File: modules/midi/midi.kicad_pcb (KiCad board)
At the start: 2 copper layers, 30.5 x 68.6 mm, 4 parts

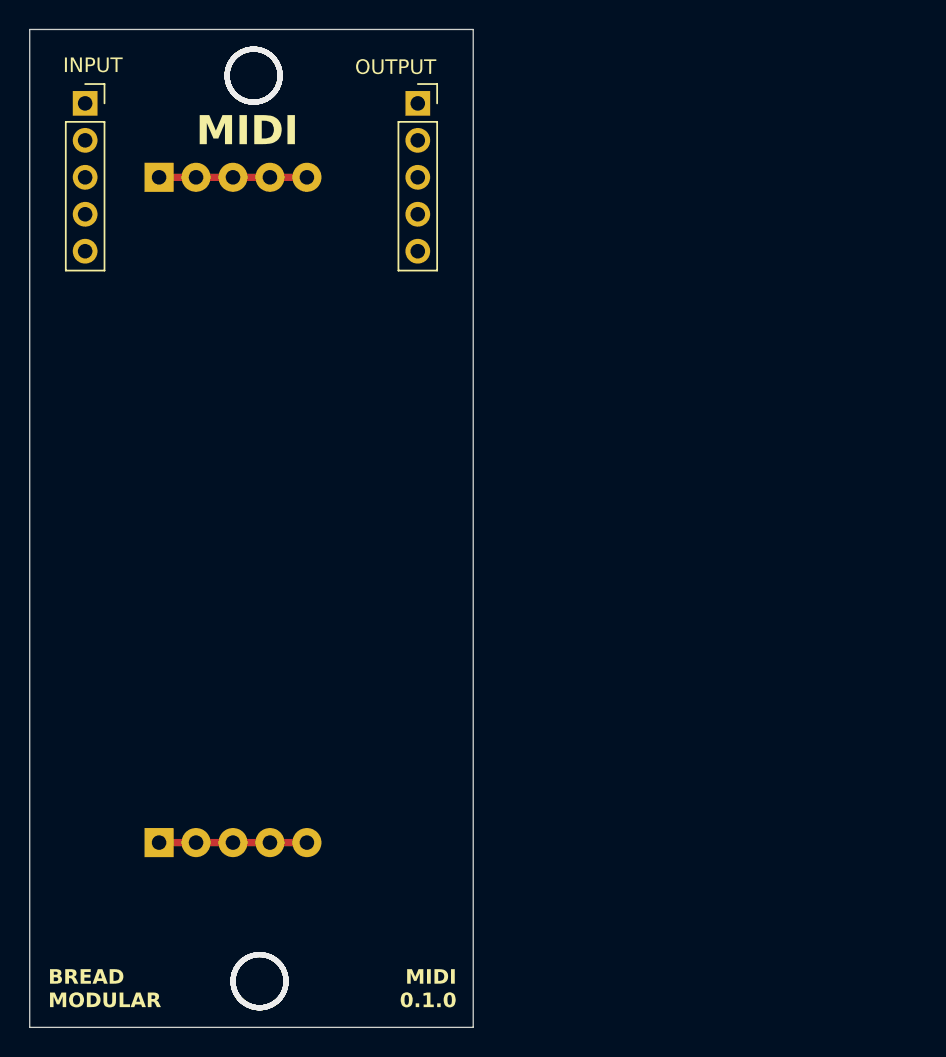
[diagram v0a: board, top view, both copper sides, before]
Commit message: Add MIDI PCB
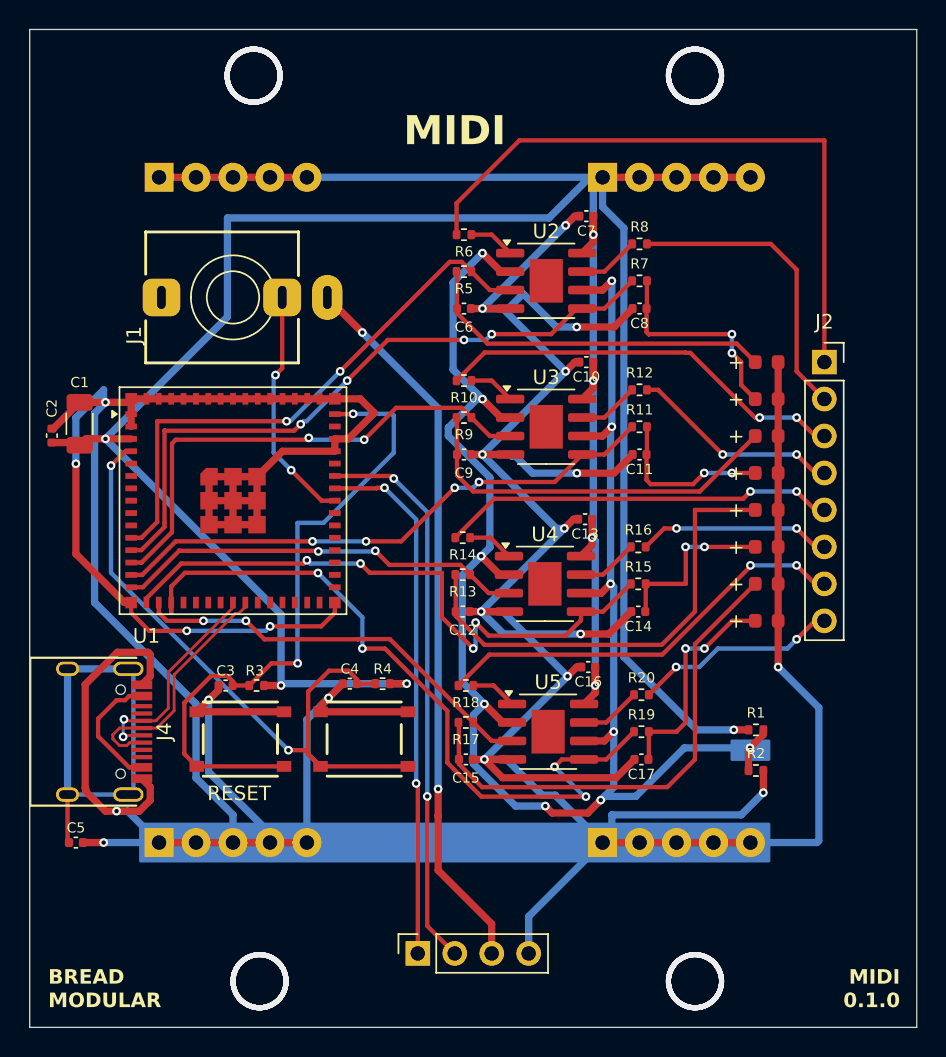
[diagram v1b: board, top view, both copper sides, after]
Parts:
- removed INPUT1, OUTPUT1: Conn_01x05_Socket, Connector_PinSocket_2.54mm:PinSocket_1x05_P2.54mm_Vertical
- added C1: 100uf, Capacitor_SMD:C_1206_3216Metric, F.Cu at (50.4, 67.7)
- added C10: 0.1uf, Capacitor_SMD:C_0402_1005Metric, F.Cu at (85.2, 63.5)
- added C11: 0.1uf, Capacitor_SMD:C_0402_1005Metric, F.Cu at (88.9, 69.8)
- added C12: 0.1uf, Capacitor_SMD:C_0402_1005Metric, F.Cu at (76.7, 80.6)
- added C13: 0.1uf, Capacitor_SMD:C_0402_1005Metric, F.Cu at (85.2, 74.3)
- added C14: 0.1uf, Capacitor_SMD:C_0402_1005Metric, F.Cu at (88.8, 80.6)
- added C15: 0.1uf, Capacitor_SMD:C_0402_1005Metric, F.Cu at (77.0, 90.8)
- added C16: 0.1uf, Capacitor_SMD:C_0402_1005Metric, F.Cu at (85.4, 84.5)
- added C17: 0.1uf, Capacitor_SMD:C_0402_1005Metric, F.Cu at (89.0, 90.8)
- added C2: 0.1uf, Capacitor_SMD:C_0402_1005Metric, F.Cu at (48.5, 68.6)
- added C3: 0.1uf, Capacitor_SMD:C_0402_1005Metric, F.Cu at (60.5, 85.7)
- added C4: 0.1uf, Capacitor_SMD:C_0402_1005Metric, F.Cu at (69.0, 85.6)
- added C5: 0.1uf, Capacitor_SMD:C_0402_1005Metric, F.Cu at (50.2, 96.5)
- added C6: 0.1uf, Capacitor_SMD:C_0402_1005Metric, F.Cu at (76.8, 59.8)
- added C7: 0.1uf, Capacitor_SMD:C_0402_1005Metric, F.Cu at (85.2, 53.5)
- added C8: 0.1uf, Capacitor_SMD:C_0402_1005Metric, F.Cu at (88.9, 59.8)
- added C9: 0.1uf, Capacitor_SMD:C_0402_1005Metric, F.Cu at (76.8, 69.8)
- added D1: LED, LED_SMD:LED_0603_1608Metric, F.Cu at (97.6, 63.5)
- added D2: LED, LED_SMD:LED_0603_1608Metric, F.Cu at (97.6, 66.0)
- added D3: LED, LED_SMD:LED_0603_1608Metric, F.Cu at (97.6, 68.6)
- added D4: LED, LED_SMD:LED_0603_1608Metric, F.Cu at (97.6, 71.1)
- added D5: LED, LED_SMD:LED_0603_1608Metric, F.Cu at (97.6, 73.7)
- added D6: LED, LED_SMD:LED_0603_1608Metric, F.Cu at (97.6, 76.2)
- added D7: LED, LED_SMD:LED_0603_1608Metric, F.Cu at (97.6, 78.7)
- added D8: LED, LED_SMD:LED_0603_1608Metric, F.Cu at (97.6, 81.3)
- added GND2: Conn_01x05_Pin, BreadModular_MISC:Power_Connector, B.Cu at (86.4, 96.5)
- added J1: AudioJack3, BreadModular_AudioJacks:Jack_3.5mm_QingPu_WQP-PJ366ST_Vertical, F.Cu at (61.0, 59.1)
- added J2: GATE_OUTS, Connector_PinSocket_2.54mm:PinSocket_1x08_P2.54mm_Vertical, F.Cu at (101.6, 63.5)
- added J3: CONFIG, Connector_PinSocket_2.54mm:PinSocket_1x04_P2.54mm_Vertical, F.Cu at (73.7, 104.1)
- added J4: USB_C_Receptacle_USB2.0_16P, BreadModular_TypeC:HRO-TYPE-C-31-M-12, F.Cu at (47.0, 88.9)
- added R1: 1k, Resistor_SMD:R_0402_1005Metric, F.Cu at (96.9, 88.8)
- added R10: 1k, Resistor_SMD:R_0402_1005Metric, F.Cu at (76.8, 64.8)
- added R11: 2k, Resistor_SMD:R_0402_1005Metric, F.Cu at (88.9, 67.9)
- added R12: 1k, Resistor_SMD:R_0402_1005Metric, F.Cu at (88.9, 65.4)
- added R13: 2k, Resistor_SMD:R_0402_1005Metric, F.Cu at (76.7, 78.1)
- added R14: 1k, Resistor_SMD:R_0402_1005Metric, F.Cu at (76.7, 75.6)
- added R15: 2k, Resistor_SMD:R_0402_1005Metric, F.Cu at (88.8, 78.7)
- added R16: 1k, Resistor_SMD:R_0402_1005Metric, F.Cu at (88.8, 76.2)
- added R17: 2k, Resistor_SMD:R_0402_1005Metric, F.Cu at (77.0, 88.3)
- added R18: 1k, Resistor_SMD:R_0402_1005Metric, F.Cu at (77.0, 85.7)
- added R19: 2k, Resistor_SMD:R_0402_1005Metric, F.Cu at (89.0, 88.9)
- added R2: 1k, Resistor_SMD:R_0402_1005Metric, F.Cu at (96.9, 91.6)
- added R20: 1k, Resistor_SMD:R_0402_1005Metric, F.Cu at (89.0, 86.4)
- added R3: 10K, Resistor_SMD:R_0402_1005Metric, F.Cu at (62.6, 85.7)
- added R4: 10K, Resistor_SMD:R_0402_1005Metric, F.Cu at (71.2, 85.6)
- added R5: 2k, Resistor_SMD:R_0402_1005Metric, F.Cu at (76.8, 57.3)
- added R6: 1k, Resistor_SMD:R_0402_1005Metric, F.Cu at (76.8, 54.7)
- added R7: 2k, Resistor_SMD:R_0402_1005Metric, F.Cu at (88.9, 57.9)
- added R8: 1k, Resistor_SMD:R_0402_1005Metric, F.Cu at (88.9, 55.4)
- added R9: 2k, Resistor_SMD:R_0402_1005Metric, F.Cu at (76.8, 67.3)
- added SW1: RESET, BreadModular_MISC:SPST_TS-1187A-B-A-B, F.Cu at (61.5, 89.4)
- added SW2: BOOT, BreadModular_MISC:SPST_TS-1187A-B-A-B, F.Cu at (70.0, 89.4)
- added U1: ESP32-S3-MINI-1U, RF_Module:ESP32-S2-MINI-1U, F.Cu at (61.0, 73.0)
- added U2: MCP6002-xSN, Package_SO:SOIC-8-1EP_3.9x4.9mm_P1.27mm_EP2.29x3mm, F.Cu at (82.5, 57.9)
- added U3: MCP6002-xSN, Package_SO:SOIC-8-1EP_3.9x4.9mm_P1.27mm_EP2.29x3mm, F.Cu at (82.5, 67.9)
- added U4: MCP6002-xSN, Package_SO:SOIC-8-1EP_3.9x4.9mm_P1.27mm_EP2.29x3mm, F.Cu at (82.4, 78.7)
- added U5: MCP6002-xSN, Package_SO:SOIC-8-1EP_3.9x4.9mm_P1.27mm_EP2.29x3mm, F.Cu at (82.6, 88.9)
- added V_SUPPLY2: Conn_01x05_Pin, BreadModular_MISC:Power_Connector, B.Cu at (86.4, 50.8)
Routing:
- net GND: track 10.2 -> 431.9 mm, vias 0 -> 21
- net V_SUPPLY: track 10.2 -> 215.8 mm, vias 0 -> 8
- net V_MID: track 0.00 -> 121.4 mm, vias 0 -> 11
- net /esp32/GATE_8: track 0.00 -> 50.6 mm, vias 0 -> 4
- net MIDI_GND: track 0.00 -> 49.8 mm, vias 0 -> 2
- net Net-(SW2-B): track 0.00 -> 46.3 mm, vias 0 -> 2
- net /esp32/GATE_2: track 0.00 -> 46.0 mm, vias 0 -> 4
- net Net-(SW1-B): track 0.00 -> 45.3 mm, vias 0 -> 2
- net /gate_process/GATE_A_OUT: track 0.00 -> 44.5 mm
- net /esp32/GATE_6: track 0.00 -> 42.8 mm, vias 0 -> 4
- net /esp32/GATE_1: track 0.00 -> 38.8 mm, vias 0 -> 2
- net /esp32/GATE_4: track 0.00 -> 38.6 mm, vias 0 -> 4
- net RX: track 0.00 -> 38.5 mm, vias 0 -> 2
- net TX: track 0.00 -> 36.4 mm, vias 0 -> 2
- net /esp32/GATE_3: track 0.00 -> 34.9 mm, vias 0 -> 2
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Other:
- board size 30.5 x 68.6 mm -> 61 x 68.6 mm
- board text added: "RESET"
- board text removed: "INPUT"
- board text removed: "OUTPUT"

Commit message: Finalized the midi module.
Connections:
- R6 pad 1: unconnected-(R6-Pad1) -> Net-(R6-Pad1)
- R8 pad 1: unconnected-(R8-Pad1) -> Net-(R8-Pad1)
- U2 pad 1: unconnected-(R6-Pad1) -> Net-(R6-Pad1)
- U2 pad 7: unconnected-(R8-Pad1) -> Net-(R8-Pad1)
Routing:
- net GND: track 431.9 -> 438.6 mm
- net V_MID: track 121.4 -> 125.8 mm
- net unconnected-(R8-Pad1): track 4.22 -> 0.00 mm
- net Net-(R8-Pad1): track 0.00 -> 4.22 mm
- net unconnected-(R6-Pad1): track 3.19 -> 0.00 mm
- net Net-(R6-Pad1): track 0.00 -> 3.19 mm
- net Net-(U1-IO19): track 15.1 -> 17.0 mm
- net Net-(U1-IO20): track 17.0 -> 15.3 mm
- net Net-(D4-A): track 11.6 -> 12.9 mm
- net Net-(D5-A): track 32.2 -> 33.4 mm
- net Net-(D2-A): track 14.6 -> 15.7 mm
- net /esp32/GATE_8: track 50.6 -> 51.6 mm
- net /esp32/GATE_4: track 38.6 -> 39.5 mm
- net Net-(D3-A): track 26.5 -> 27.3 mm
- net /esp32/GATE_2: track 46.0 -> 46.7 mm
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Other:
- board text added: "1"
- board text added: "2"
- board text added: "3"
- board text added: "4"
- board text added: "5"
- board text added: "6"
- board text added: "7"
- board text added: "8"
- board text added: "GATE CHANNEL"

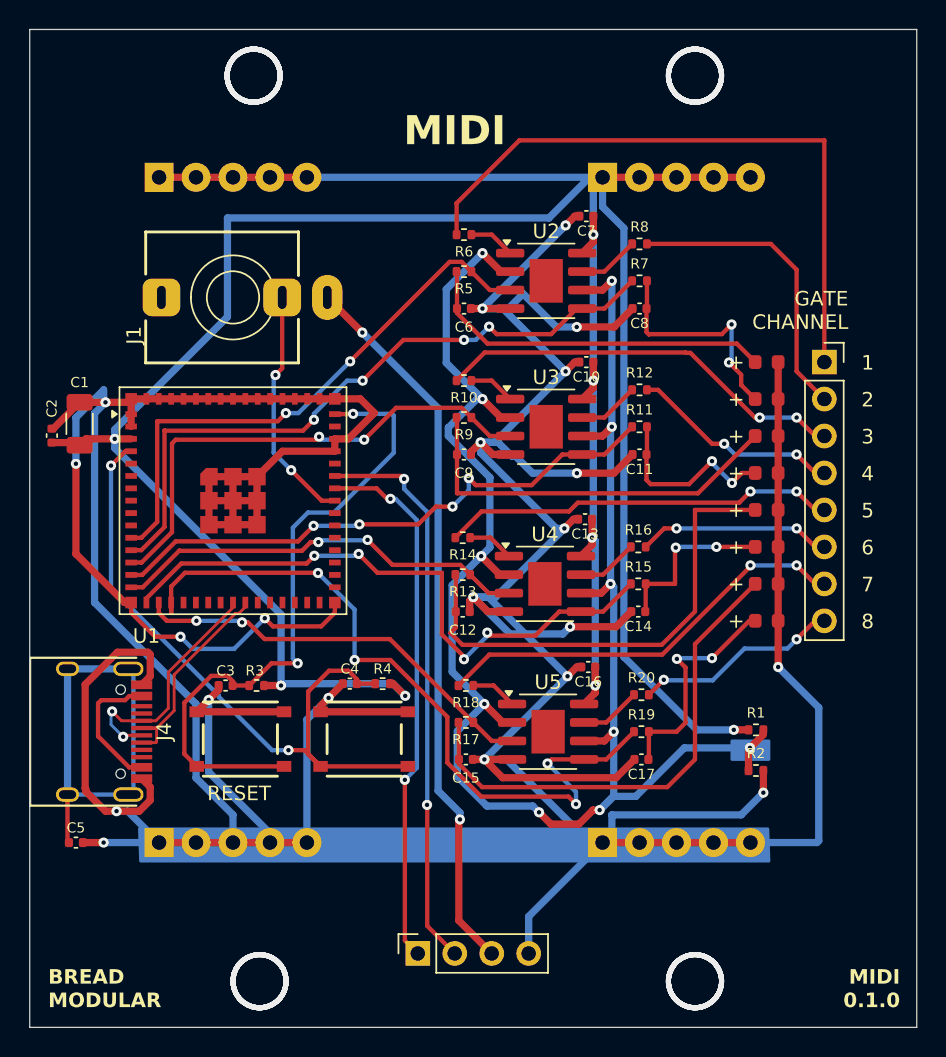
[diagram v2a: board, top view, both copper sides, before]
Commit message: Implement the PCB layout and routing
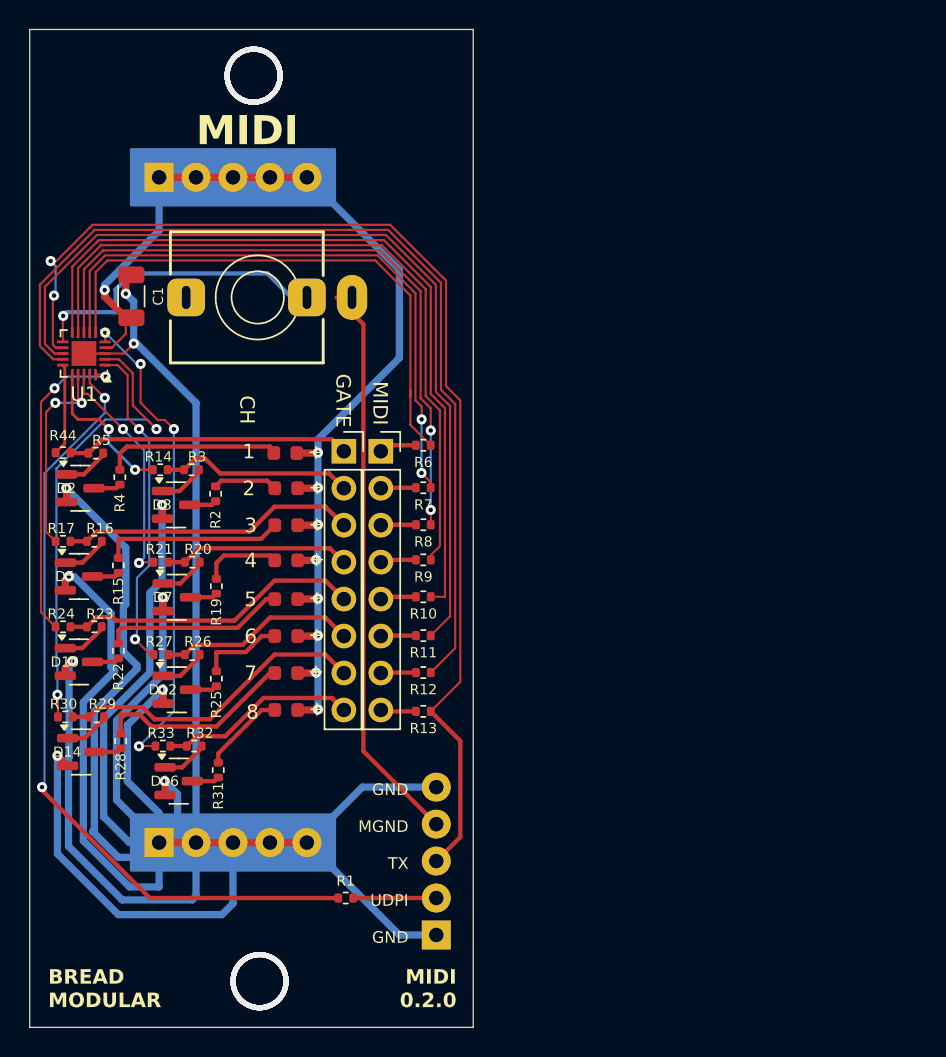
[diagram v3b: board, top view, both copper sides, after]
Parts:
- removed C10, C11, C12, C13, C14, C15, C16, C17, C2, C3, C4, C5, C6, C7, C8, C9: 0.1uf, Capacitor_SMD:C_0402_1005Metric
- removed GND2, V_SUPPLY2: Conn_01x05_Pin, BreadModular_MISC:Power_Connector
- removed J2: GATE_OUTS, Connector_PinSocket_2.54mm:PinSocket_1x08_P2.54mm_Vertical
- removed J3: CONFIG, Connector_PinSocket_2.54mm:PinSocket_1x04_P2.54mm_Vertical
- removed J4: USB_C_Receptacle_USB2.0_16P, BreadModular_TypeC:HRO-TYPE-C-31-M-12
- removed R18: 1k, Resistor_SMD:R_0402_1005Metric
- removed SW1: RESET, BreadModular_MISC:SPST_TS-1187A-B-A-B
- removed SW2: BOOT, BreadModular_MISC:SPST_TS-1187A-B-A-B
- removed U2, U3, U4, U5: MCP6002-xSN, Package_SO:SOIC-8-1EP_3.9x4.9mm_P1.27mm_EP2.29x3mm
- added CONFIG1: Conn_01x05_Pin, BreadModular_MISC:Power_Connector, B.Cu at (74.9, 102.9)
- added D10: SS8050, Package_TO_SOT_SMD:SOT-23, F.Cu at (50.4, 84.1)
- added D100: LED, LED_SMD:LED_0603_1608Metric, F.Cu at (64.6, 69.8)
- added D11: LED, LED_SMD:LED_0603_1608Metric, F.Cu at (64.6, 82.3)
- added D12: SS8050, Package_TO_SOT_SMD:SOT-23, F.Cu at (57.1, 86.0)
- added D13: LED, LED_SMD:LED_0603_1608Metric, F.Cu at (64.6, 84.9)
- added D14: SS8050, Package_TO_SOT_SMD:SOT-23, F.Cu at (50.5, 90.3)
- added D15: LED, LED_SMD:LED_0603_1608Metric, F.Cu at (64.6, 87.4)
- added D16: SS8050, Package_TO_SOT_SMD:SOT-23, F.Cu at (57.2, 92.3)
- added OUTPUT1: GATE_OUT, Connector_PinSocket_2.54mm:PinSocket_1x08_P2.54mm_Vertical, F.Cu at (68.6, 69.6)
- added OUTPUT2: MIDI_OUT, Connector_PinSocket_2.54mm:PinSocket_1x08_P2.54mm_Vertical, F.Cu at (71.1, 69.6)
- added R21: 1k, Resistor_SMD:R_0402_1005Metric, F.Cu at (56.0, 77.2)
- added R22: 1k, Resistor_SMD:R_0402_1005Metric, F.Cu at (53.1, 83.3)
- added R23: 10k, Resistor_SMD:R_0402_1005Metric, F.Cu at (51.4, 81.7)
- added R24: 1k, Resistor_SMD:R_0402_1005Metric, F.Cu at (49.3, 81.7)
- added R25: 1k, Resistor_SMD:R_0402_1005Metric, F.Cu at (59.8, 85.3)
- added R26: 10k, Resistor_SMD:R_0402_1005Metric, F.Cu at (58.2, 83.6)
- added R27: 1k, Resistor_SMD:R_0402_1005Metric, F.Cu at (56.0, 83.6)
- added R28: 1k, Resistor_SMD:R_0402_1005Metric, F.Cu at (53.2, 89.5)
- added R29: 10k, Resistor_SMD:R_0402_1005Metric, F.Cu at (51.6, 87.9)
- added R30: 1k, Resistor_SMD:R_0402_1005Metric, F.Cu at (49.4, 87.9)
- added R31: 1k, Resistor_SMD:R_0402_1005Metric, F.Cu at (59.9, 91.5)
- added R32: 10k, Resistor_SMD:R_0402_1005Metric, F.Cu at (58.3, 89.9)
- added R33: 1k, Resistor_SMD:R_0402_1005Metric, F.Cu at (56.1, 89.9)
- added R44: 1k, Resistor_SMD:R_0402_1005Metric, F.Cu at (49.3, 69.7)
- D2, D3, D5, D7: value LED -> SS8050; footprint LED_SMD:LED_0603_1608Metric -> Package_TO_SOT_SMD:SOT-23
- J1: value AudioJack3 -> MIDI_IN
- R1: value 1k -> 4.7k
- R11, R13, R15, R17, R19, R7, R9: value 2k -> 1k
- R16, R20: value 1k -> 10k
- R3: value 10K -> 10k
- R4: value 10K -> 1k
- R5: value 2k -> 10k
- U1: value ESP32-S3-MINI-1U -> ATtiny1616-M; footprint RF_Module:ESP32-S2-MINI-1U -> Package_DFN_QFN:VQFN-20-1EP_3x3mm_P0.4mm_EP1.7x1.7mm
- moved D2 47.6 mm to (50.5, 72.2), turned to 0 degrees
- moved D5 47.5 mm to (50.4, 78.2), turned to 0 degrees
- moved R2 41.7 mm to (59.8, 72.6), turned to 90 degrees
- moved D3 40.9 mm to (57.1, 73.3), turned to 0 degrees
- moved D7 40.5 mm to (57.1, 79.7), turned to 0 degrees
- moved R16 37.4 mm to (51.4, 75.8)
- moved R15 35.7 mm to (53.1, 77.5), turned to 90 degrees
- moved D1 34.1 mm to (64.6, 72.2), turned to 0 degrees
- moved D4 33.2 mm to (64.6, 74.7), turned to 0 degrees
- moved D8 33.1 mm to (64.6, 79.8), turned to 0 degrees
- moved D6 33.0 mm to (64.6, 77.1), turned to 0 degrees
- moved R20 32.2 mm to (58.2, 77.2)
- moved R19 30.9 mm to (59.8, 78.9), turned to 90 degrees
- moved R1 30.5 mm to (68.7, 100.3)
- moved R17 30.4 mm to (49.3, 75.8), turned to 0 degrees
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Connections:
- net /esp32/GATE_7 renamed GATE_3
- C1 pad 1: V_SUPPLY -> GND
- C1 pad 2: GND -> V_SUPPLY
- D1 pad 1: GND -> Net-(D1-K)
- D1 pad 2: Net-(D1-A) -> V_SUPPLY
- D2 pad 1: GND -> Net-(D2-K-Pad1)
- D2 pad 2: Net-(D2-A) -> GND
- D3 pad 1: GND -> Net-(D3-K-Pad1)
- D3 pad 2: Net-(D3-A) -> GND
- D4 pad 1: GND -> Net-(D4-K)
- D4 pad 2: Net-(D4-A) -> V_SUPPLY
- D5 pad 1: GND -> Net-(D5-K-Pad1)
- D5 pad 2: Net-(D5-A) -> GND
- D6 pad 1: GND -> Net-(D6-K)
- D6 pad 2: Net-(D6-A) -> V_SUPPLY
- D7 pad 1: GND -> Net-(D7-K-Pad1)
- D7 pad 2: Net-(D7-A) -> GND
- D8 pad 1: GND -> Net-(D8-K)
- D8 pad 2: Net-(D8-A) -> V_SUPPLY
- J1 pad R: /esp32/MIDI_IN -> MIDI_IN
- J1 pad S: MIDI_GND -> MIDI_GROUND
- R1 pad 1: V_SUPPLY -> Net-(U1-~{RESET}/PA0)
- R1 pad 2: V_MID -> UDPI
- R10 pad 1: Net-(R10-Pad1) -> MIDI_OUT_5
- R10 pad 2: /gate_process1/GATE_A_OUT -> Net-(OUTPUT2-Pin_5)
- R11 pad 1: /esp32/GATE_4 -> MIDI_OUT_6
- R11 pad 2: Net-(D4-A) -> Net-(OUTPUT2-Pin_6)
- R12 pad 1: Net-(R12-Pad1) -> MIDI_OUT_7
- R12 pad 2: /gate_process1/GATE_B_OUT -> Net-(OUTPUT2-Pin_7)
- R13 pad 1: /esp32/GATE_5 -> TX
- R13 pad 2: Net-(D5-A) -> Net-(OUTPUT2-Pin_8)
- R14 pad 1: Net-(R14-Pad1) -> GATE_2
- R14 pad 2: /gate_process2/GATE_A_OUT -> /Gate Out1/GATE_OUT
- R15 pad 1: /esp32/GATE_6 -> Net-(D5-A)
- R15 pad 2: Net-(D6-A) -> Net-(D4-K)
- R16 pad 1: Net-(R16-Pad1) -> /Gate Out2/GATE_OUT
- R16 pad 2: /gate_process2/GATE_B_OUT -> Net-(D5-K-Pad1)
- R17 pad 2: Net-(D7-A) -> /Gate Out2/GATE_OUT
- R19 pad 1: /esp32/GATE_8 -> Net-(D7-A)
- R19 pad 2: Net-(D8-A) -> Net-(D6-K)
- R2 pad 1: V_MID -> Net-(D3-A)
- R2 pad 2: GND -> Net-(D1-K)
- R20 pad 1: Net-(R20-Pad1) -> /Gate Out3/GATE_OUT
- R20 pad 2: /gate_process3/GATE_B_OUT -> Net-(D7-K-Pad1)
- R3 pad 1: V_SUPPLY -> /Gate Out1/GATE_OUT
- R3 pad 2: Net-(SW1-B) -> Net-(D3-K-Pad1)
- R4 pad 1: V_SUPPLY -> Net-(D2-A)
- R4 pad 2: Net-(SW2-B) -> Net-(D100-K)
- R5 pad 1: /esp32/GATE_1 -> /Gate Out/GATE_OUT
- R5 pad 2: Net-(D1-A) -> Net-(D2-K-Pad1)
- R6 pad 1: Net-(R6-Pad1) -> MIDI_OUT_1
- R6 pad 2: /gate_process/GATE_A_OUT -> Net-(OUTPUT2-Pin_1)
- R7 pad 1: /esp32/GATE_2 -> MIDI_OUT_2
- R7 pad 2: Net-(D2-A) -> Net-(OUTPUT2-Pin_2)
- R8 pad 1: Net-(R8-Pad1) -> MIDI_OUT_3
- R8 pad 2: /gate_process/GATE_B_OUT -> Net-(OUTPUT2-Pin_3)
- R9 pad 1: /esp32/GATE_3 -> MIDI_OUT_4
- R9 pad 2: Net-(D3-A) -> Net-(OUTPUT2-Pin_4)
- U1 pad 1: GND -> GATE_6
- U1 pad 10: unconnected-(U1-IO6-Pad10) -> MIDI_OUT_5
- U1 pad 11: /esp32/GATE_1 -> MIDI_IN
- U1 pad 12: /esp32/GATE_2 -> TX
- U1 pad 13: /esp32/GATE_3 -> MIDI_OUT_6
- U1 pad 14: /esp32/GATE_4 -> MIDI_OUT_7
- U1 pad 15: /esp32/GATE_5 -> GATE_1
- U1 pad 16: /esp32/GATE_6 -> GATE_2
- U1 pad 18: /esp32/GATE_8 -> GATE_4
- U1 pad 19: unconnected-(U1-IO15-Pad19) -> Net-(U1-~{RESET}/PA0)
- U1 pad 2: GND -> GATE_7
- U1 pad 20: unconnected-(U1-IO16-Pad20) -> GATE_5
- U1 pad 21: unconnected-(U1-IO17-Pad21) -> GND
- U1 pad 3: V_SUPPLY -> GND
- U1 pad 4: Net-(SW2-B) -> V_SUPPLY
- U1 pad 5: unconnected-(U1-IO1-Pad5) -> GATE_8
- U1 pad 6: unconnected-(U1-IO2-Pad6) -> MIDI_OUT_1
- U1 pad 7: unconnected-(U1-IO3-Pad7) -> MIDI_OUT_2
- U1 pad 8: unconnected-(U1-IO4-Pad8) -> MIDI_OUT_3
- U1 pad 9: unconnected-(U1-IO5-Pad9) -> MIDI_OUT_4
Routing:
- net GND: track 438.6 -> 264.4 mm, vias 21 -> 10
- net V_SUPPLY: track 215.8 -> 77.5 mm, vias 8 -> 9
- net V_MID: track 125.8 -> 0.00 mm, vias 11 -> 0
- net MIDI_OUT_7: track 0.00 -> 64.7 mm
- net MIDI_OUT_6: track 0.00 -> 60.2 mm
- net Net-(U1-~{RESET}/PA0): track 0.00 -> 54.2 mm, vias 0 -> 2
- net MIDI_OUT_5: track 0.00 -> 53.9 mm
- net /esp32/GATE_8: track 51.6 -> 0.00 mm, vias 4 -> 0
- net MIDI_GND: track 49.8 -> 0.00 mm, vias 2 -> 0
- net MIDI_OUT_4: track 0.00 -> 49.4 mm
- net Net-(SW2-B): track 47.0 -> 0.00 mm, vias 2 -> 0
- net /esp32/GATE_2: track 46.7 -> 0.00 mm, vias 4 -> 0
- net Net-(SW1-B): track 45.5 -> 0.00 mm, vias 2 -> 0
- net MIDI_OUT_3: track 0.00 -> 45.5 mm, vias 0 -> 2
- net /gate_process/GATE_A_OUT: track 44.5 -> 0.00 mm
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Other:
- board size 61 x 68.6 mm -> 30.5 x 68.6 mm
- board text added: "CH"
- board text added: "GATE"
- board text added: "GND"
- board text added: "MGND"
- board text added: "MIDI 0.2.0"
- board text added: "TX"
- board text added: "UDPI"
- board text removed: "GATE CHANNEL"
- board text removed: "MIDI 0.1.0"
- board text removed: "RESET"

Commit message: midi: Add support to select MIDI A or B
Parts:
- CONFIG1: footprint BreadModular_MISC:Power_Connector -> BreadModular_MISC:Conn_Holes_6
- moved CONFIG1 0.63 mm to (74.9, 103.5)
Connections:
- CONFIG1 pad 1: GND -> UDPI
- CONFIG1 pad 2: UDPI -> TX
- CONFIG1 pad 3: TX -> MIDI_GROUND
- CONFIG1 pad 4: MIDI_GROUND -> MIDI_DATA_TYPE_A
- CONFIG1 pad 5: GND -> MIDI_IN
- J1 pad R: MIDI_IN -> MIDI_DATA_TYPE_B
- J1 pad T: unconnected-(J1-PadT) -> MIDI_DATA_TYPE_A
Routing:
- net MIDI_DATA_TYPE_A: track 0.00 -> 50.0 mm
- net MIDI_DATA_TYPE_B: track 0.00 -> 41.8 mm
- net MIDI_IN: track 20.3 -> 55.3 mm, vias 1 -> 3
- net GND: track 264.4 -> 242.4 mm
- net MIDI_GROUND: track 39.0 -> 42.3 mm
- net TX: track 79.6 -> 82.1 mm
- net UDPI: track 5.72 -> 7.08 mm
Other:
- board text added: "MIDI 0.3.0"
- board text added: "MIDI IN"
- board text added: "TYPE: A"
- board text added: "TYPE: B"
- board text removed: "GND"
- board text removed: "MIDI 0.2.0"
